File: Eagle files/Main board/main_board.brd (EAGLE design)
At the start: 58 x 90 mm, 65 parts, among them X1 ARK2, X2 ARK1

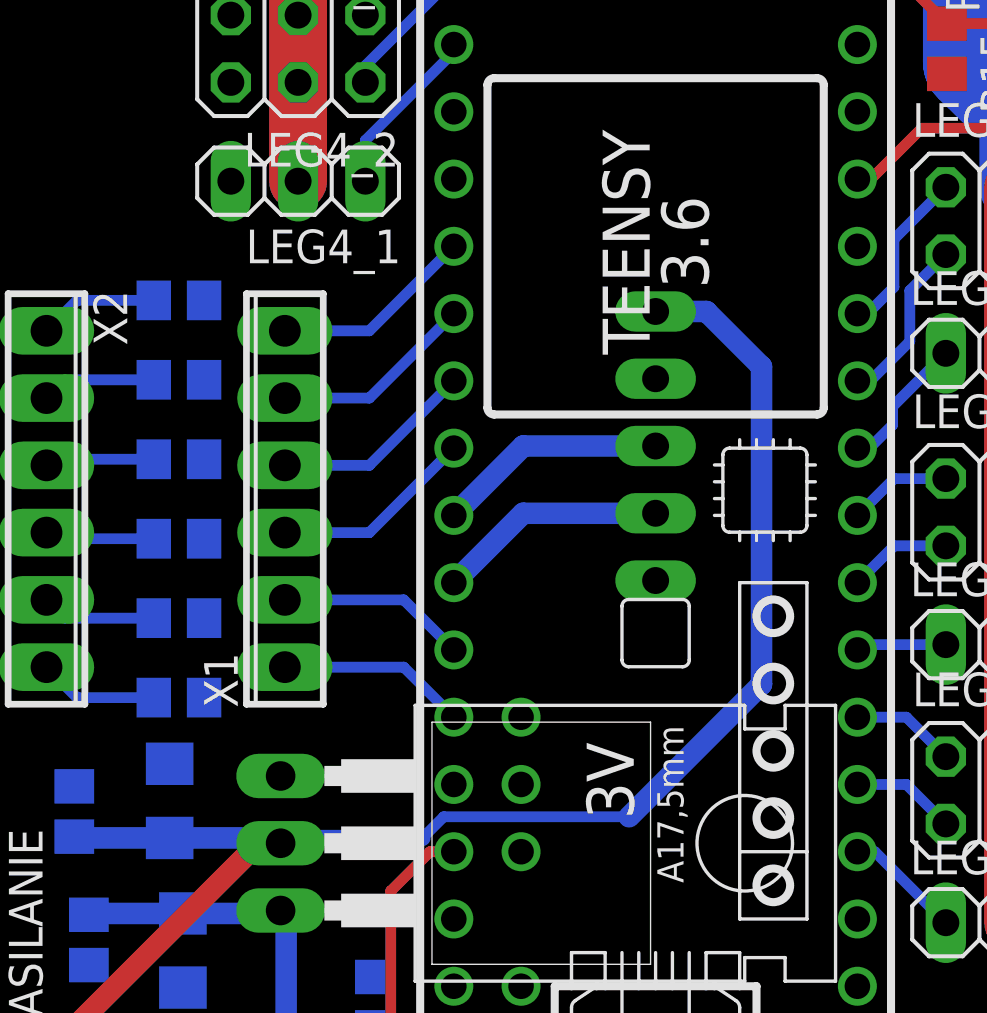
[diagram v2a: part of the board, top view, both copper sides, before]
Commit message: Update main_board.brd
Move MPU position
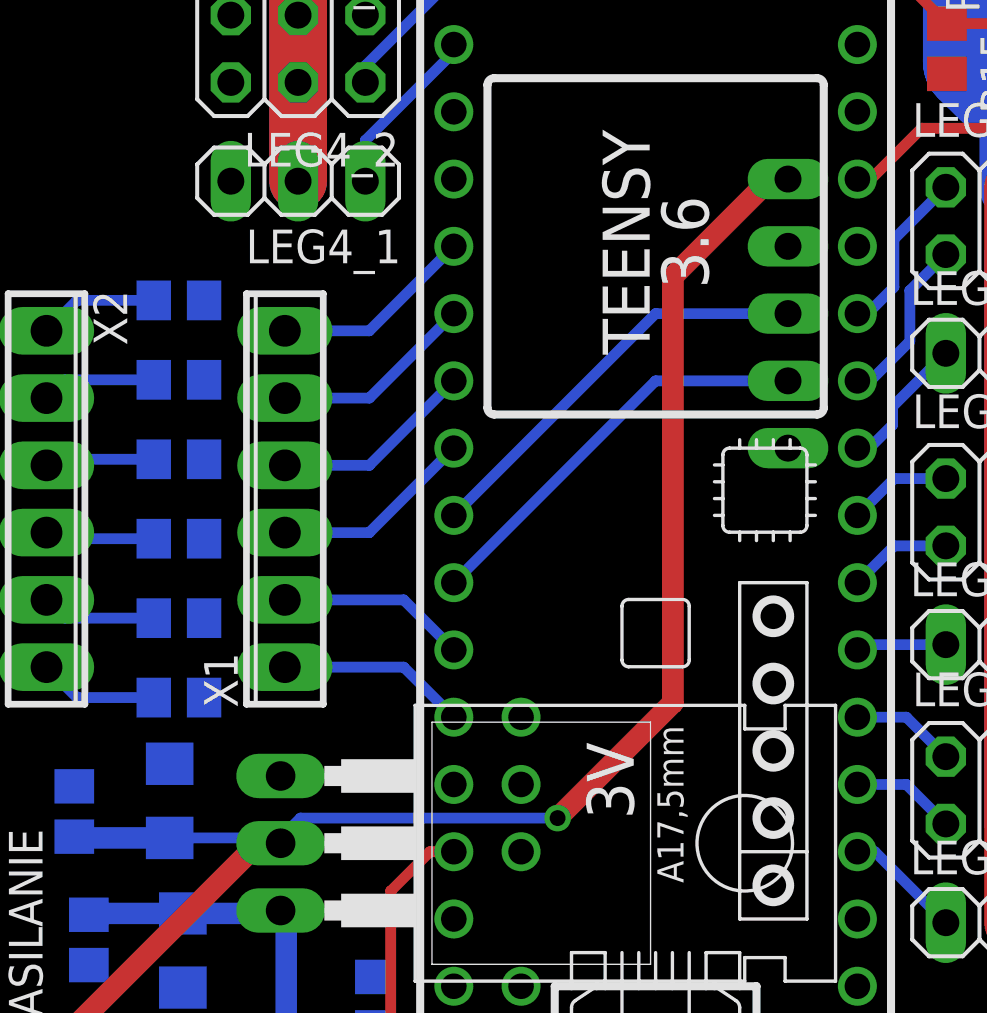
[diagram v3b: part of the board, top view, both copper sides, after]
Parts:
- moved MPU6050 7.07 mm to (5.00, 0.00)
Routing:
- net SDA: track 8.71 -> 15.8 mm
- net SCL: track 8.71 -> 15.8 mm
- net +3V3: track 58.3 -> 59.6 mm, vias 0 -> 1
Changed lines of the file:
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@@
 <grid distance="1" unitdist="mm" unit="mm" style="lines" multiple="1" display="no" altdistance="0.05" altunitdist="mm" altunit="mm"/>
 <layers>
-<layer number="1" name="Top" color="4" fill="1" visible="no" active="yes"/>
+<layer number="1" name="Top" color="4" fill="1" visible="yes" active="yes"/>
 <layer number="2" name="Route2" color="1" fill="3" visible="no" active="no"/>
 <layer number="3" name="Route3" color="4" fill="3" visible="no" active="no"/>
@@
 <element name="LEG6_1" library="pinhead" package="1X03" value="" x="-13.5" y="25" rot="R180"/>
 <element name="LEG6_2" library="pinhead" package="2X03" value="" x="-13.5" y="30" rot="R180"/>
-<element name="MPU6050" library="pinhead" package="1X05" value="6EOF" x="0" y="-5" rot="MR270"/>
+<element name="MPU6050" library="pinhead" package="1X05" value="6EOF" x="5" y="0" rot="MR270"/>
 <element name="R3" library="rcl" package="R0805" value="510r" x="-19.96" y="-35.03" rot="R180"/>
 <element name="TEENSY41" library="teensy" package="TEENSY_3.5/3.6_BASIC" value="TEENSY_3.5/3.6_BASIC" x="0" y="0" rot="R90"/>
@@
 <contactref element="MPU6050" pad="1"/>
 <contactref element="3V" pad="2"/>
-<wire x1="-18.35" y1="-19.8" x2="-14.36" y2="-19.8" width="0.8128" layer="16"/>
-<wire x1="-14.36" y1="-19.8" x2="-14.16" y2="-20" width="0.8128" layer="16"/>
 <wire x1="-18.35" y1="-19.8" x2="-21.9" y2="-19.8" width="0.8128" layer="16"/>
 <wire x1="-21.9" y1="-19.8" x2="-21.95" y2="-19.75" width="0.8128" layer="16"/>
-<wire x1="-14.36" y1="-19.8" x2="-8.8" y2="-19.8" width="0.6096" layer="16"/>
-<wire x1="0" y1="0.08" x2="1.92" y2="0.08" width="0.8128" layer="16"/>
-<wire x1="1.92" y1="0.08" x2="4" y2="-2" width="0.8128" layer="16"/>
-<wire x1="4" y1="-2" x2="4" y2="-14" width="0.8128" layer="16"/>
-<wire x1="4" y1="-14" x2="-1" y2="-19" width="0.8128" layer="16"/>
 <wire x1="-22.15" y1="-28.94" x2="-22.15" y2="-27.15" width="0.8128" layer="1"/>
 <wire x1="-22.15" y1="-27.15" x2="-15" y2="-20" width="0.8128" layer="1"/>
+<wire x1="-18.35" y1="-19.8" x2="-14.16" y2="-19.8" width="0.4064" layer="16"/>
+<wire x1="-14.16" y1="-19.8" x2="-14.16" y2="-20" width="0.4064" layer="16"/>
 <wire x1="-15" y1="-20" x2="-14.16" y2="-20" width="0.8128" layer="1"/>
-<wire x1="-8.8" y1="-19.8" x2="-8" y2="-19" width="0.4064" layer="16"/>
-<wire x1="-8" y1="-19" x2="-1" y2="-19" width="0.4064" layer="16"/>
+<wire x1="-14.16" y1="-19.8" x2="-13.41" y2="-19.05" width="0.4064" layer="16"/>
+<wire x1="-13.41" y1="-19.05" x2="-3.7" y2="-19.05" width="0.4064" layer="16"/>
+<via x="-3.7" y="-19.05" extent="1-16" drill="0.6" shape="square"/>
+<wire x1="-3.7" y1="-19.05" x2="0.65" y2="-14.7" width="0.8128" layer="1"/>
+<wire x1="0.65" y1="-14.7" x2="0.65" y2="1.4" width="0.8128" layer="1"/>
+<wire x1="0.65" y1="1.4" x2="4.33" y2="5.08" width="0.8128" layer="1"/>
+<wire x1="4.33" y1="5.08" x2="5" y2="5.08" width="0.8128" layer="1"/>
 </signal>
 <signal name="GND">
@@
 <contactref element="MPU6050" pad="4"/>
 <contactref element="TEENSY41" pad="19/A5/SCL"/>
-<wire x1="0" y1="-7.54" x2="-5" y2="-7.54" width="0.8128" layer="16"/>
-<wire x1="-5" y1="-7.54" x2="-7.62" y2="-10.16" width="0.8128" layer="16"/>
+<wire x1="-7.62" y1="-10.16" x2="0" y2="-2.54" width="0.4064" layer="16"/>
+<wire x1="0" y1="-2.54" x2="5" y2="-2.54" width="0.4064" layer="16"/>
 </signal>
 <signal name="SDA">
 <contactref element="MPU6050" pad="3"/>
 <contactref element="TEENSY41" pad="18/A4/SDA"/>
-<wire x1="0" y1="-5" x2="-5" y2="-5" width="0.8128" layer="16"/>
-<wire x1="-5" y1="-5" x2="-7.62" y2="-7.62" width="0.8128" layer="16"/>
+<wire x1="-7.62" y1="-7.62" x2="0" y2="0" width="0.4064" layer="16"/>
+<wire x1="0" y1="0" x2="5" y2="0" width="0.4064" layer="16"/>
 </signal>
 <signal name="+BAT">
